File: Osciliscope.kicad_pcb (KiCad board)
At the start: 2 copper layers, 135.1 x 85.3 mm, 5 parts, among them J2 Conn_ARM_JTAG_SWD_20, U1 STM32H753VITx, X1 X322525MOB4SI

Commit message: Brick all of it
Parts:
- added C1: 100n, Capacitor_SMD:C_0402_1005Metric, F.Cu at (133.0, 90.6)
- added C10: 100n, Capacitor_SMD:C_0402_1005Metric, F.Cu at (138.7, 92.6)
- added C11: 100n, Capacitor_SMD:C_0402_1005Metric, F.Cu at (138.7, 94.5)
- added C12: 100n, Capacitor_SMD:C_0402_1005Metric, F.Cu at (138.7, 96.5)
- added C13: 100n, Connector_PinHeader_1.00mm:PinHeader_1x01_P1.00mm_Vertical, F.Cu at (117.4, 85.0)
- added C2: 100n, Capacitor_SMD:C_0402_1005Metric, F.Cu at (133.0, 92.6)
- added C3: 100n, Capacitor_SMD:C_0402_1005Metric, F.Cu at (133.0, 94.5)
- added C4: 100n, Capacitor_SMD:C_0402_1005Metric, F.Cu at (133.0, 96.5)
- added C5: 2.2u, Capacitor_SMD:C_0402_1005Metric, F.Cu at (135.8, 90.6)
- added C6: 2.2u, Capacitor_SMD:C_0402_1005Metric, F.Cu at (135.8, 92.6)
- added C7: 0.1u, Capacitor_SMD:C_0402_1005Metric, F.Cu at (135.8, 94.5)
- added C8: 3.9pf, Capacitor_SMD:C_0402_1005Metric, F.Cu at (135.8, 96.5)
- added C9: 3.9pf, Capacitor_SMD:C_0402_1005Metric, F.Cu at (138.7, 90.6)
- added H1: MountingHole_Pad, Connector_PinHeader_1.00mm:PinHeader_1x01_P1.00mm_Vertical, F.Cu at (117.4, 88.1)
- added H2: MountingHole_Pad, Connector_PinHeader_1.00mm:PinHeader_1x01_P1.00mm_Vertical, F.Cu at (120.7, 85.0)
- added H3: MountingHole_Pad, Connector_PinHeader_1.00mm:PinHeader_1x01_P1.00mm_Vertical, F.Cu at (120.7, 88.1)
- added H4: MountingHole_Pad, Connector_PinHeader_1.00mm:PinHeader_1x01_P1.00mm_Vertical, F.Cu at (124.0, 85.0)
- added H5: MountingHole_Pad, Connector_PinHeader_1.00mm:PinHeader_1x01_P1.00mm_Vertical, F.Cu at (124.0, 88.1)
- added H6: MountingHole_Pad, Connector_PinHeader_1.00mm:PinHeader_1x01_P1.00mm_Vertical, F.Cu at (127.4, 85.0)
- added H7: MountingHole_Pad, Connector_PinHeader_1.00mm:PinHeader_1x01_P1.00mm_Vertical, F.Cu at (127.4, 88.1)
- added J1: USB_C_Receptacle_USB2.0_14P, Connector_USB:USB_C_Receptacle_Amphenol_12401610E4-2A, F.Cu at (82.0, 66.5)
- added R1: 10k, Resistor_SMD:R_0603_1608Metric, F.Cu at (129.5, 90.9)
- added R2: 5.1k, Resistor_SMD:R_0603_1608Metric, F.Cu at (129.5, 93.4)
- added R3: 5.1k, Resistor_SMD:R_0603_1608Metric, F.Cu at (129.5, 95.9)
- added R5: 22, Resistor_SMD:R_0603_1608Metric, F.Cu at (129.5, 98.4)
- added R6: 22, Resistor_SMD:R_0603_1608Metric, F.Cu at (129.5, 100.9)
- moved J2 51.6 mm to (141.2, 56.9)
- moved S1 27.2 mm to (82.8, 55.9)
- moved X1 12.9 mm to (99.7, 65.9), turned to 180 degrees
- moved U1 12.9 mm to (110.7, 65.0)
- moved R4 6.43 mm to (114.8, 77.7)
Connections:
- U1 pad 70: unconnected-(U1-PA11-Pad70) -> D-
- U1 pad 71: unconnected-(U1-PA12-Pad71) -> D+
- U1 pad 72: unconnected-(U1-PA13-Pad72) -> SWDIO
- U1 pad 76: unconnected-(U1-PA14-Pad76) -> SWCLK
- U1 pad 77: unconnected-(U1-PA15-Pad77) -> JTDI
- U1 pad 89: unconnected-(U1-PB3-Pad89) -> TRACESWO
- U1 pad 90: unconnected-(U1-PB4-Pad90) -> NJTRST

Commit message: Basic PCB
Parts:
- removed C10, C11, C12, C4: 100n, Capacitor_SMD:C_0402_1005Metric
- removed C13: 100n, Connector_PinHeader_1.00mm:PinHeader_1x01_P1.00mm_Vertical
- removed C5, C6: 2.2u, Capacitor_SMD:C_0402_1005Metric
- removed C7: 0.1u, Capacitor_SMD:C_0402_1005Metric
- removed C8, C9: 3.9pf, Capacitor_SMD:C_0402_1005Metric
- removed H1, H2, H3, H4, H5, H6, H7: MountingHole_Pad, Connector_PinHeader_1.00mm:PinHeader_1x01_P1.00mm_Vertical
- removed R3: 5.1k, Resistor_SMD:R_0603_1608Metric
- removed S1: Tactile Button, 160gf, PCM_JLCPCB:SW-SMD_4P-L5.1-W5.1-P3.70-LS6.5-TL-2
- removed X1: X322525MOB4SI, PCM_JLCPCB:OSC-SMD_4P-L3.2-W2.5-BL
- added J3: U.FL, Connector_Coaxial:BNC_Amphenol_031-5539_Vertical, F.Cu at (142.7, 125.0)
- added R7: 1M, Resistor_SMD:R_1210_3225Metric, F.Cu at (183.5, 121.0)
- added R8: 1M, Resistor_SMD:R_1210_3225Metric, F.Cu at (183.5, 125.2)
- added R9: 1M, Resistor_SMD:R_1210_3225Metric, F.Cu at (183.5, 129.4)
- added SW1: SW_Rotary_1x8_MP, Rotary_Encoder:RotaryEncoder_Alps_EC11E-Switch_Vertical_H20mm_CircularMountingHoles, F.Cu at (138.8, 77.5)
- added SW2: SW_Rotary_1x8_MP, Rotary_Encoder:RotaryEncoder_Alps_EC11E-Switch_Vertical_H20mm_CircularMountingHoles, F.Cu at (161.2, 78.3)
- added U2: ADC082S101, Package_SO:VSSOP-8_3x3mm_P0.65mm, F.Cu at (152.9, 101.8)
- added U3: TLV9061xDBV, Package_TO_SOT_SMD:SOT-23-5, F.Cu at (163.4, 109.8)
- added U5: TLV9061xDBV, Package_TO_SOT_SMD:SOT-23-5, F.Cu at (147.5, 109.1)
- C1, C2, C3: value 100n -> 1uF; footprint Capacitor_SMD:C_0402_1005Metric -> Capacitor_SMD:C_1206_3216Metric
- J1: value USB_C_Receptacle_USB2.0_14P -> U.FL; footprint Connector_USB:USB_C_Receptacle_Amphenol_12401610E4-2A -> Connector_Coaxial:BNC_Amphenol_031-5539_Vertical
- J2: value Conn_ARM_JTAG_SWD_20 -> Conn_01x04_Socket; footprint Connector_PinSocket_2.54mm:PinSocket_2x10_P2.54mm_Vertical -> Connector_PinHeader_2.00mm:PinHeader_1x04_P2.00mm_Vertical
- R1: value 10k -> 1M; footprint Resistor_SMD:R_0603_1608Metric -> Resistor_SMD:R_1206_3216Metric
- R2: value 5.1k -> 1M; footprint Resistor_SMD:R_0603_1608Metric -> Resistor_SMD:R_1210_3225Metric
- R4: value 1k -> 1M; footprint Resistor_SMD:R_0603_1608Metric -> Resistor_SMD:R_1210_3225Metric
- R5, R6: value 22 -> 1M; footprint Resistor_SMD:R_0603_1608Metric -> Resistor_SMD:R_1210_3225Metric
- U1: value STM32H753VITx -> MCP1700x-330xxMB; footprint Package_QFP:LQFP-100_14x14mm_P0.5mm -> Package_TO_SOT_SMD:SOT-89-3
- moved J1 103.6 mm to (167.3, 125.4), turned to 0 degrees
- moved R4 75.2 mm to (183.5, 108.3)
- moved U1 64.0 mm to (166.4, 96.6), turned to 90 degrees
- moved R6 56.3 mm to (183.5, 116.8)
- moved R5 55.8 mm to (183.5, 112.6)
- moved R2 55.1 mm to (183.5, 104.1)
- moved R1 54.8 mm to (183.5, 100.4)
- moved J2 49.9 mm to (127.4, 104.8), turned to 180 degrees
- moved C3 38.7 mm to (171.6, 96.9), turned to -90 degrees
- moved C1 21.5 mm to (154.1, 94.6)
- moved C2 13.6 mm to (146.5, 91.4)
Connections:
- C1 pad 1: VDD -> 5Vin
- C2 pad 1: VDD -> 3.3Vo
- C3 pad 1: VDD -> 3.3Vo
- J2 pad 1: unconnected-(J2-VTREF-Pad1) -> RPI_CS
- J2 pad 2: unconnected-(J2-VCC/NC-Pad2) -> RPI_SCLK
- J2 pad 3: unconnected-(J2-~{TRST}-Pad3) -> RPI_DIN
- J2 pad 4: Net-(J2-GND-Pad10) -> RPI_DOUT
- R1 pad 1: GND -> RAW_IN_1
- R1 pad 2: Net-(U1-BOOT0) -> GND
- R2 pad 1: Net-(J1-CC1) -> RAW_IN_2
- R4 pad 1: VDD -> Net-(U3-+)
- R4 pad 2: Net-(U1-VBAT) -> GND
- R5 pad 1: Net-(J1-D--PadA7) -> CHAN_1
- R5 pad 2: D- -> Net-(U3--)
- R6 pad 1: Net-(J1-D+-PadA6) -> RAW_IN_1
- R6 pad 2: D+ -> Net-(U3--)
- U1 pad 1: unconnected-(U1-PE2-Pad1) -> GND
- U1 pad 2: unconnected-(U1-PE3-Pad2) -> 5Vin
- U1 pad 3: unconnected-(U1-PE4-Pad3) -> 3.3Vo
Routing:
- net RPI_DIN: track 0.00 -> 36.2 mm, vias 0 -> 2
- net RPI_DOUT: track 0.00 -> 35.3 mm
- net RPI_SCLK: track 0.00 -> 30.5 mm
- net RPI_CS: track 0.00 -> 26.8 mm
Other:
- board size 135.1 x 85.3 mm -> 54.6 x 107.4 mm

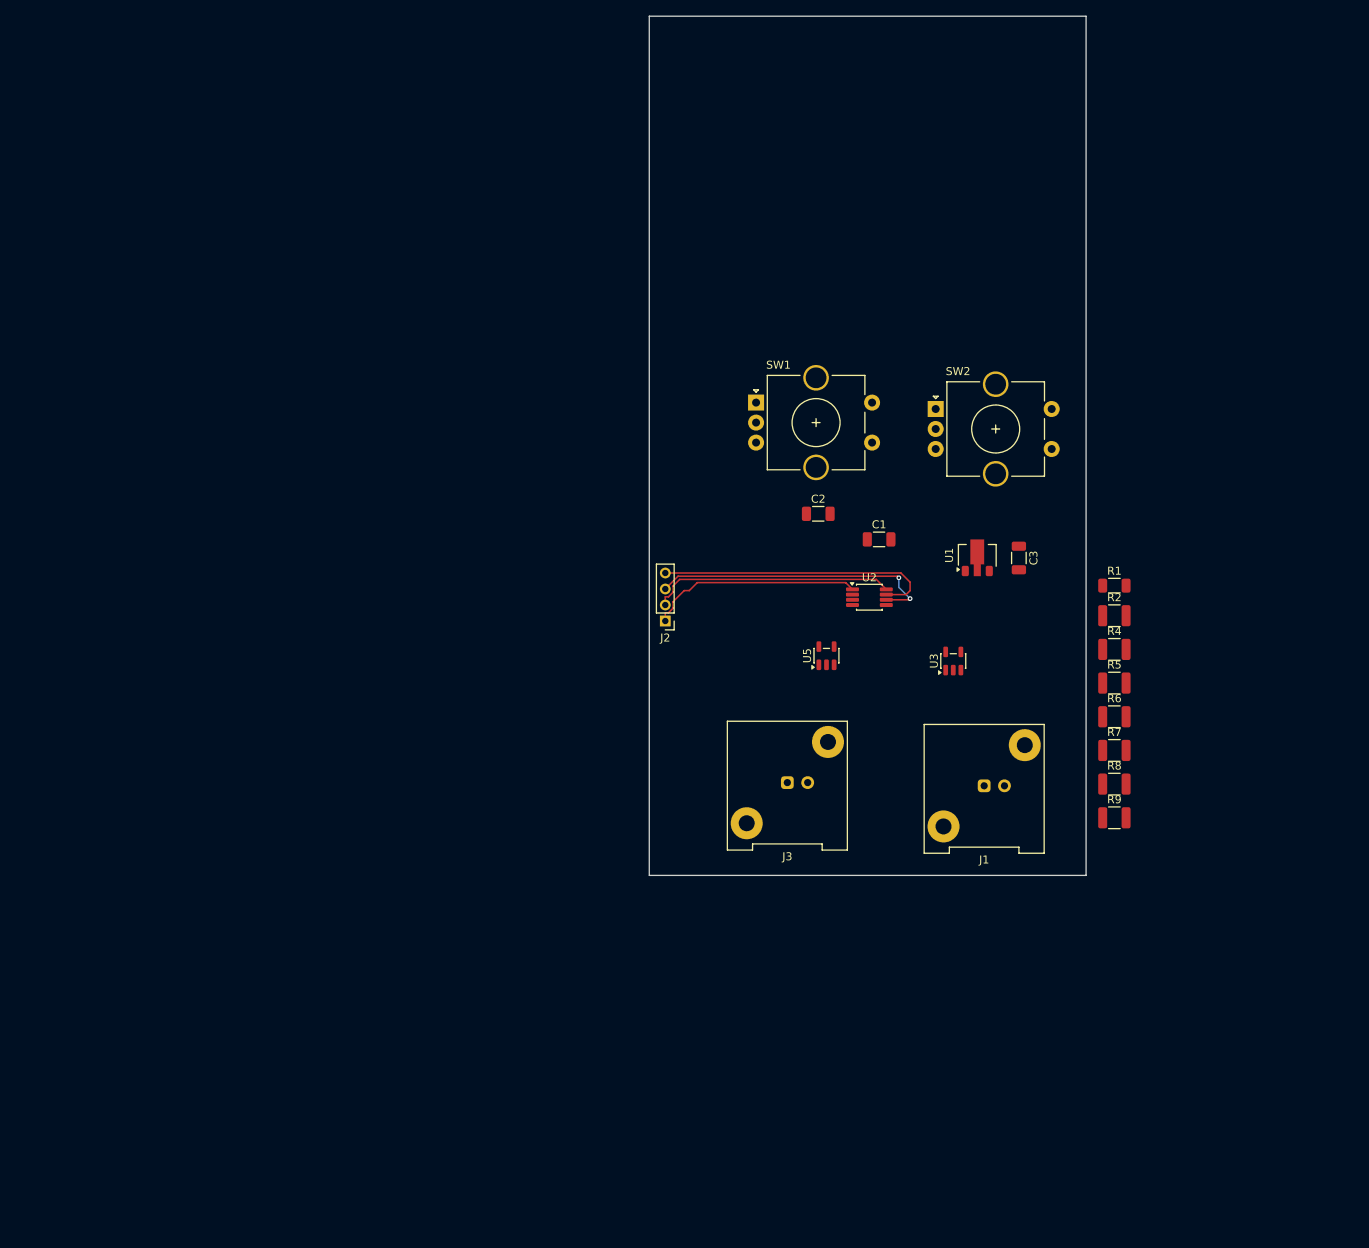
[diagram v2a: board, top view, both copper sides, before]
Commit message: Added new op amp design
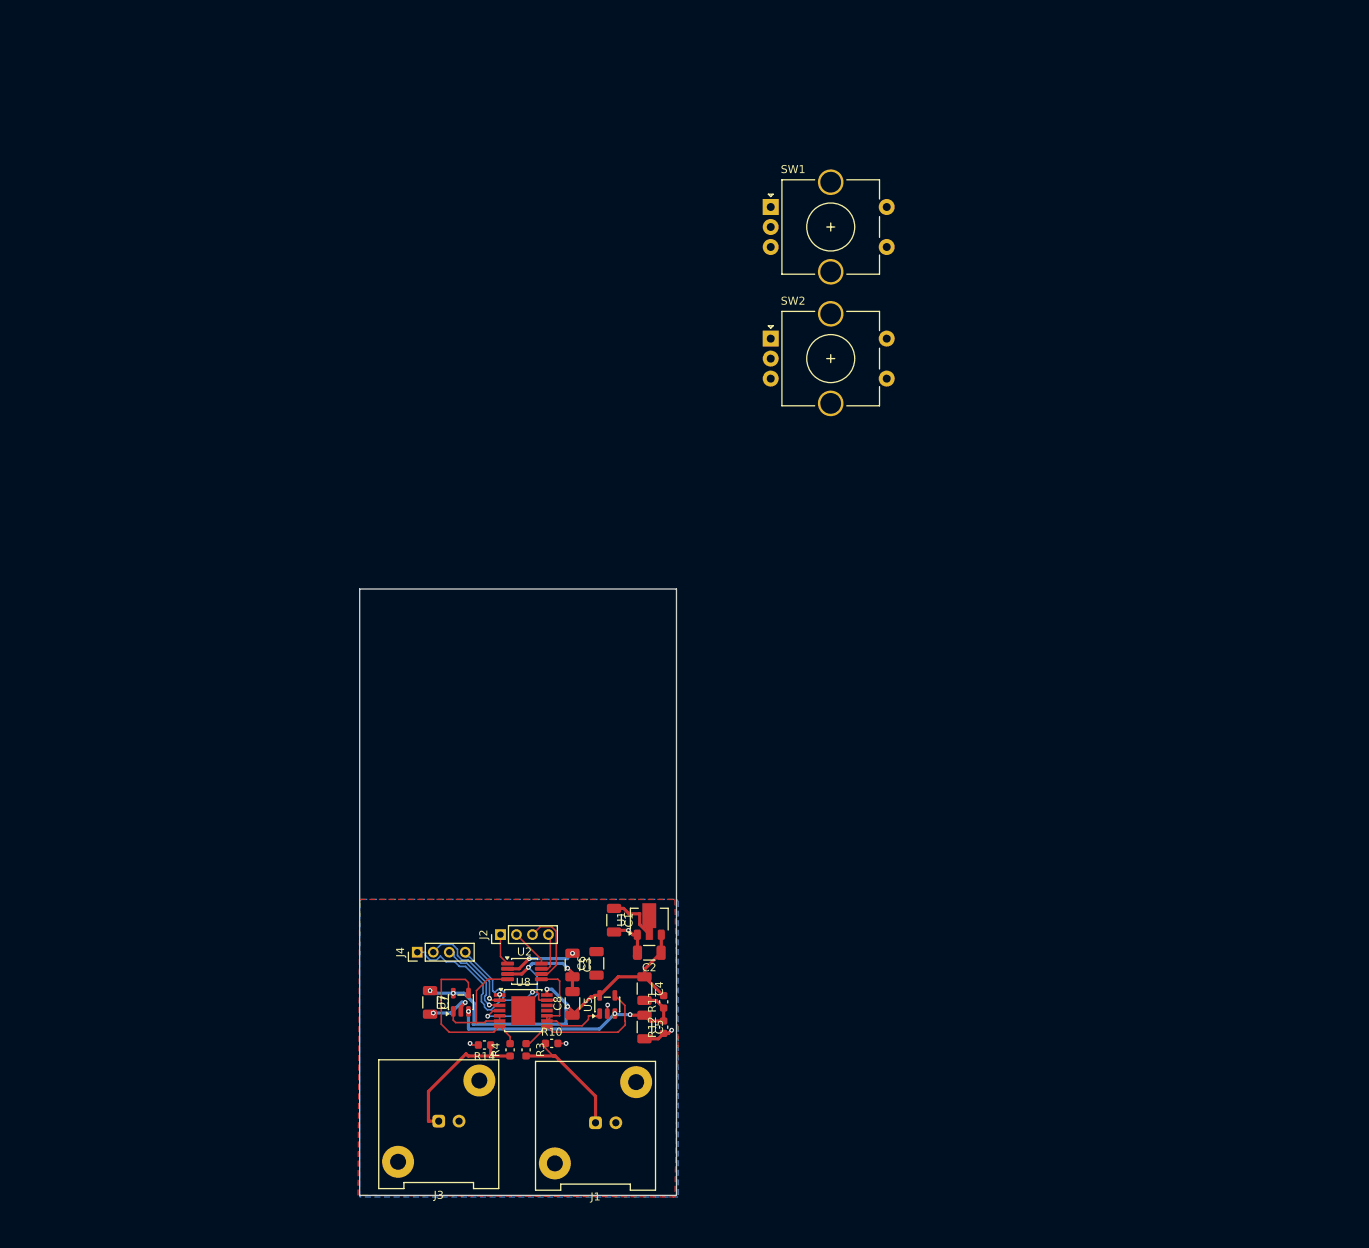
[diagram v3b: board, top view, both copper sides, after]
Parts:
- removed R1: 1M, Resistor_SMD:R_1206_3216Metric
- removed R2, R5, R6, R7, R8, R9: 1M, Resistor_SMD:R_1210_3225Metric
- removed U3: TLV9061xDBV, Package_TO_SOT_SMD:SOT-23-5
- added C4: 1uF, Capacitor_SMD:C_1206_3216Metric, F.Cu at (124.8, 150.8)
- added C5: 1uF, Capacitor_SMD:C_1206_3216Metric, F.Cu at (124.8, 155.6)
- added C6: 1uF, Capacitor_SMD:C_1206_3216Metric, F.Cu at (118.8, 147.6)
- added C7: 1uF, Capacitor_SMD:C_1206_3216Metric, F.Cu at (98.0, 152.5)
- added C8: 1uF, Capacitor_SMD:C_1206_3216Metric, F.Cu at (115.8, 152.6)
- added J4: Conn_01x04_Socket, Connector_PinHeader_2.00mm:PinHeader_1x04_P2.00mm_Vertical, F.Cu at (96.4, 146.2)
- added R10: 1M, Capacitor_SMD:C_0603_1608Metric, F.Cu at (113.2, 157.6)
- added R11: 10k, Capacitor_SMD:C_0603_1608Metric, F.Cu at (127.2, 152.4)
- added R12: 10k, Capacitor_SMD:C_0603_1608Metric, F.Cu at (127.2, 155.6)
- added R14: 1M, Capacitor_SMD:C_0603_1608Metric, F.Cu at (104.8, 157.8)
- added R3: 5k, Capacitor_SMD:C_0603_1608Metric, F.Cu at (110.0, 158.4)
- added U7: TLV9061xDBV, Package_TO_SOT_SMD:SOT-23-5, F.Cu at (101.9, 152.5)
- added U8: MCP4251-104E/ML-ND, Package_SO:TSSOP-14-1EP_4.4x5mm_P0.65mm, F.Cu at (109.7, 153.5)
- R4: value 1M -> 5k; footprint Resistor_SMD:R_1210_3225Metric -> Capacitor_SMD:C_0603_1608Metric
- moved R4 90.6 mm to (108.0, 158.4), turned to -90 degrees
- moved C3 75.5 mm to (115.8, 147.8)
- moved J1 64.3 mm to (118.7, 167.5)
- moved U2 63.6 mm to (109.8, 148.6)
- moved U1 61.2 mm to (125.4, 142.1)
- moved J3 60.7 mm to (99.1, 167.3)
- moved C2 58.8 mm to (125.4, 146.3), turned to 180 degrees
- moved C1 58.0 mm to (121.0, 142.2), turned to -90 degrees
- moved U5 51.5 mm to (120.1, 152.7)
- moved J2 44.3 mm to (106.8, 144.0), turned to 90 degrees
- moved SW1 24.5 mm to (140.6, 53.0)
- moved SW2 22.4 mm to (140.6, 69.5)
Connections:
- C2 pad 1: 3.3Vo -> V3.3
- J1 pad 1: RAW_IN_1 -> Net-(J1-In)
- J3 pad 1: RAW_IN_2 -> Net-(J3-In)
- R4 pad 1: Net-(U3-+) -> C2_G_IN
- R4 pad 2: GND -> Net-(J3-In)
- U1 pad 3: 3.3Vo -> V3.3
- U2 pad 4: CHAN_2 -> C2_G_OUT
- U2 pad 5: CHAN_1 -> C1_G_OUT
- U5 pad 1: CHAN_2 -> C1_G_OUT
- U5 pad 2: unconnected-(U5-V--Pad2) -> GND
- U5 pad 3: Net-(U5-+) -> V1.8
- U5 pad 4: Net-(U5--) -> C1_G_IN
- U5 pad 5: unconnected-(U5-V+-Pad5) -> V3.3
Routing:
- net V3.3: track 0.00 -> 49.3 mm, vias 0 -> 4
- net GND: track 0.00 -> 43.5 mm, vias 0 -> 10
- net V1.8: track 0.00 -> 32.2 mm, vias 0 -> 3
- net RPI_DOUT: track 35.3 -> 5.31 mm
- net RPI_DIN: track 36.2 -> 10.2 mm, vias 2 -> 0
- net RPI_SCLK: track 30.5 -> 4.91 mm
- net RPI_CS: track 26.8 -> 3.99 mm
- net C2_G_IN: track 0.00 -> 21.2 mm
- net Net-(J3-In): track 0.00 -> 18.8 mm
- net C1_G_OUT: track 0.00 -> 17.9 mm
- net C1_G_IN: track 0.00 -> 17.8 mm
- net RPI_DOUT_DP: track 0.00 -> 17.3 mm, vias 0 -> 1
- net RPI_CS_DP: track 0.00 -> 17.0 mm, vias 0 -> 1
- net C2_G_OUT: track 0.00 -> 16.2 mm
- net Net-(J1-In): track 0.00 -> 15.7 mm
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- added copper zone on B.Cu, net GND
- added copper zone on F.Cu, net GND
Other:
- board size 54.6 x 107.4 mm -> 39.6 x 75.8 mm

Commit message: PCB design
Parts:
- added SW3: SW_Nidec_CAS-120A1, Button_Switch_SMD:Nidec_Copal_CAS-120A, F.Cu at (48.2, 156.8)
- added SW4: SW_Nidec_CAS-120A1, Button_Switch_SMD:Nidec_Copal_CAS-120A, F.Cu at (53.6, 156.8)
- moved C2 55.9 mm to (69.5, 145.8), turned to 0 degrees
- moved C4 55.4 mm to (69.5, 152.5), turned to 0 degrees
- moved C5 55.3 mm to (69.5, 155.9), turned to 0 degrees
- moved R11 53.4 mm to (74.3, 159.7), turned to 0 degrees
- moved R12 53.3 mm to (74.3, 162.2), turned to 0 degrees
- moved C1 51.5 mm to (69.5, 142.5), turned to 0 degrees
- moved C6 50.7 mm to (69.5, 159.2), turned to 0 degrees
- moved C8 48.2 mm to (69.5, 165.9), turned to 0 degrees
- moved C3 46.4 mm to (69.5, 149.2), turned to 0 degrees
- moved U1 44.6 mm to (84.8, 160.6), turned to 0 degrees
- moved R3 36.3 mm to (74.3, 152.1), turned to 0 degrees
- moved R4 33.9 mm to (74.3, 154.6), turned to 0 degrees
- moved J2 32.5 mm to (74.3, 142.8), turned to 0 degrees
- moved C7 30.3 mm to (69.5, 162.6), turned to 0 degrees
- moved J4 18.4 mm to (78.4, 142.8), turned to 0 degrees
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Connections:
- C3 pad 1: 3.3Vo -> V3.3
- R3 pad 2: Net-(J1-In) -> Net-(D1-A)
- R4 pad 2: Net-(J3-In) -> Net-(D3-A)
- U2 pad 2: 3.3Vo -> V3.3
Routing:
- net V3.3: track 49.3 -> 0.00 mm, vias 4 -> 0
- net GND: track 43.5 -> 0.00 mm, vias 10 -> 0
- net V1.8: track 32.2 -> 0.00 mm, vias 3 -> 0
- net C2_G_IN: track 21.2 -> 0.00 mm
- net Net-(J3-In): track 18.8 -> 0.00 mm
- net C1_G_OUT: track 17.9 -> 0.00 mm
- net C1_G_IN: track 17.8 -> 0.00 mm
- net RPI_DOUT_DP: track 17.3 -> 0.00 mm, vias 1 -> 0
- net RPI_CS_DP: track 17.0 -> 0.00 mm, vias 1 -> 0
- net C2_G_OUT: track 16.2 -> 0.00 mm
- net Net-(J1-In): track 15.7 -> 0.00 mm
- net RPI_SCLK_DP: track 13.3 -> 0.00 mm, vias 1 -> 0
- net RPI_DIN_DP: track 11.1 -> 0.00 mm, vias 1 -> 0
- net RPI_DIN: track 10.2 -> 0.00 mm
- net 3.3Vo: track 8.92 -> 0.00 mm, vias 2 -> 0
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
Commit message: USBC PD
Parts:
- added C10: 1u, Capacitor_SMD:C_1206_3216Metric, F.Cu at (95.1, 157.0)
- added C11: 1uF, Capacitor_SMD:C_1206_3216Metric, F.Cu at (114.4, 145.2)
- added C12: 10u, Capacitor_SMD:C_1206_3216Metric, F.Cu at (106.9, 135.2)
- added C13: 10u, Capacitor_SMD:C_1206_3216Metric, F.Cu at (91.6, 136.8)
- added C9: 1u, Capacitor_SMD:C_1206_3216Metric, F.Cu at (117.6, 156.9)
- added D1: D, Diode_SMD:D_0201_0603Metric, F.Cu at (121.4, 152.9)
- added D2: D, Diode_SMD:D_0201_0603Metric, F.Cu at (124.1, 152.9)
- added D3: D, Diode_SMD:D_0201_0603Metric, F.Cu at (91.8, 154.1)
- added D4: D, Diode_SMD:D_0201_0603Metric, F.Cu at (89.5, 154.1)
- added D5: Red, PCM_JLCPCB:D_0805, F.Cu at (89.0, 135.8)
- added J5: USB_C_Receptacle_USB2.0_14P, Connector_USB:USB_C_Receptacle_Amphenol_124019772112A, F.Cu at (120.6, 139.0)
- added J6: Conn_01x02_MountingPin, Connector_PinHeader_2.00mm:PinHeader_1x02_P2.00mm_Vertical, F.Cu at (87.2, 139.8)
- added R13: 10k, Capacitor_SMD:C_0603_1608Metric, F.Cu at (89.6, 139.8)
- added U3: IP2721, Package_SO:TSSOP-16_4.4x5mm_P0.65mm, F.Cu at (112.6, 138.2)
- added U4: AZ1084-5.0, Package_TO_SOT_SMD:TO-252-2, F.Cu at (98.0, 137.6)
- moved SW3 74.7 mm to (122.8, 156.8)
- moved C3 48.6 mm to (117.9, 152.9)
- moved R3 48.1 mm to (122.4, 150.8)
- moved J2 40.6 mm to (106.3, 167.8)
- moved C4 40.2 mm to (109.4, 156.8)
- moved SW4 37.4 mm to (91.0, 158.4)
- moved C5 34.6 mm to (104.0, 156.8)
- moved R11 33.2 mm to (107.1, 154.4)
- moved C8 32.3 mm to (97.0, 149.1)
- moved C7 32.0 mm to (97.0, 146.2)
- moved C6 31.9 mm to (97.0, 143.2)
- moved R12 29.9 mm to (103.2, 154.4)
- moved J4 25.6 mm to (103.9, 144.1), turned to 90 degrees
- moved C1 21.9 mm to (91.3, 143.1)
- moved C2 18.0 mm to (87.4, 147.4), turned to 90 degrees
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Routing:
- net V3.3: track 0.00 -> 74.4 mm, vias 0 -> 4
- net USBCRAW: track 0.00 -> 35.9 mm
- net 5Vin: track 0.00 -> 28.1 mm
- net V1.8: track 0.00 -> 19.2 mm, vias 0 -> 2
- net C1_G_IN: track 0.00 -> 19.2 mm, vias 0 -> 2
- net C2_G_OUT: track 0.00 -> 18.6 mm, vias 0 -> 2
- net C1_G_OUT: track 0.00 -> 18.2 mm, vias 0 -> 2
- net RPI_DOUT: track 0.00 -> 18.1 mm, vias 0 -> 2
- net Net-(J3-In): track 0.00 -> 17.7 mm
- net RPI_DIN_DP: track 0.00 -> 17.3 mm, vias 0 -> 2
- net Net-(J1-In): track 0.00 -> 16.7 mm
- net C2_G_IN: track 0.00 -> 16.6 mm
- net RPI_DIN: track 0.00 -> 14.3 mm, vias 0 -> 2
- net GND: track 0.00 -> 14.1 mm, vias 0 -> 11
- net Net-(D3-A): track 0.00 -> 13.2 mm
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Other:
- board size 39.6 x 75.8 mm -> 39.6 x 60.2 mm
